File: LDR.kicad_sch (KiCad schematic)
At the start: 8 parts, among them J1101 LDR, J1102 ter, J1103 ter, U1101 LM393

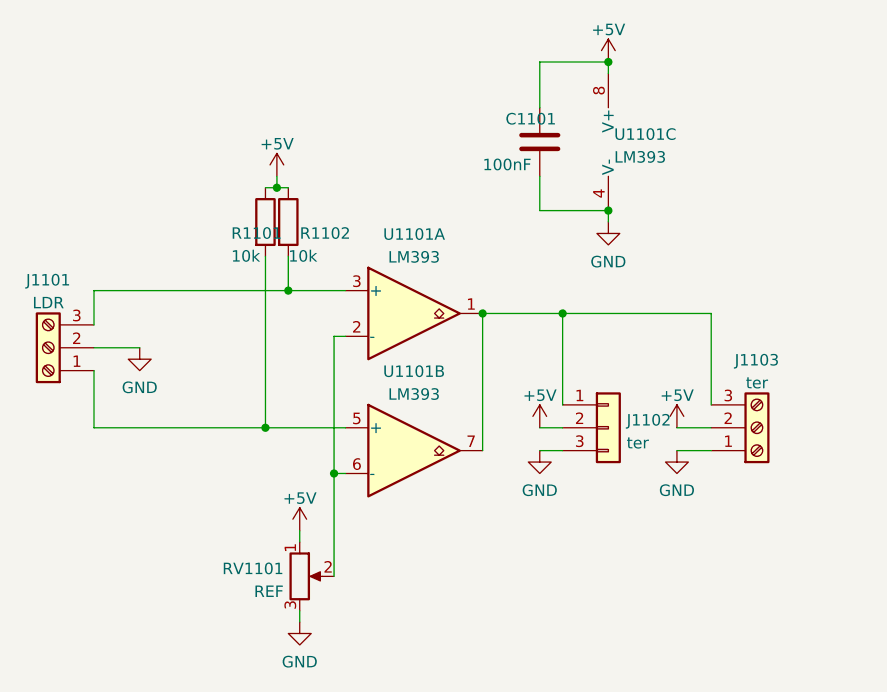
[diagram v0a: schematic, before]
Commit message: added hierarchial labels to some schematics
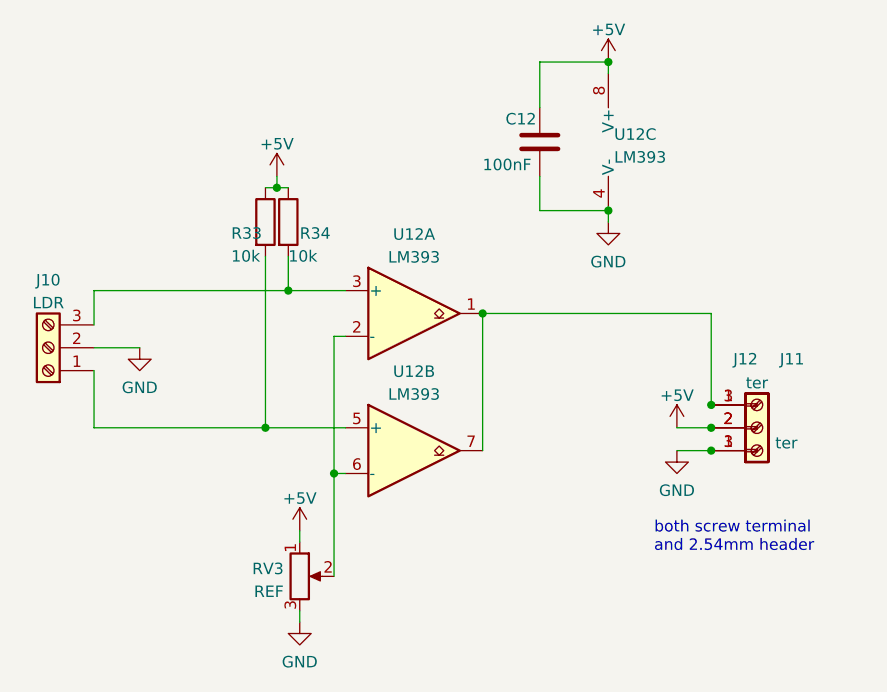
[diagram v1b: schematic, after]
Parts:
- renumbered C1101 to C12, J1101 to J10, J1102 to J11, J1103 to J12, R1101 to R33, R1102 to R34, RV1101 to RV3, U1101 to U12
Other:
- note added: "both screw terminal and 2.54mm header"
- moved on the sheet: J11

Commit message: moved some schematic scheets to their own folders and routed a board with it. This allow for re-use of PCB parts.
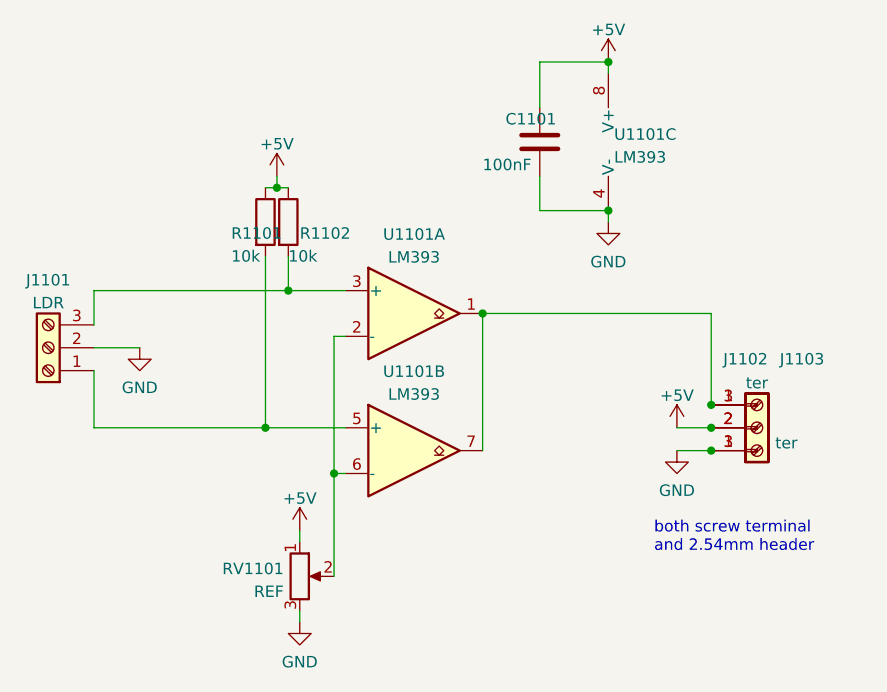
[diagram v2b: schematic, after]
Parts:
- renumbered C12 to C1101, J10 to J1101, J12 to J1102, J11 to J1103, R33 to R1101, R34 to R1102, RV3 to RV1101, U12 to U1101
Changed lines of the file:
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@@
   (symbol (lib_id "power:GND") (at 93.98 87.63 0) (unit 1)
     (in_bom yes) (on_board yes) (dnp no) (fields_autoplaced)
-    (property "Reference" "#PWR042" (at 93.98 93.98 0)
+    (property "Reference" "#PWR0132" (at 93.98 93.98 0)
       (effects (font (size 1.27 1.27)) hide)
     )
@@
       (project "general_schematics"
         (path "/e777d9ec-d073-4229-a9e6-2cf85636e407/38d599ac-34a4-48d6-818e-d419faf54082"
-          (reference "#PWR042") (unit 1)
+          (reference "#PWR0132") (unit 1)
         )
       )
@@
   (symbol (lib_id "power:+5V") (at 146.05 55.88 0) (unit 1)
     (in_bom yes) (on_board yes) (dnp no) (fields_autoplaced)
-    (property "Reference" "#PWR039" (at 146.05 59.69 0)
+    (property "Reference" "#PWR0126" (at 146.05 59.69 0)
       (effects (font (size 1.27 1.27)) hide)
     )
@@
       (project "general_schematics"
         (path "/e777d9ec-d073-4229-a9e6-2cf85636e407/38d599ac-34a4-48d6-818e-d419faf54082"
-          (reference "#PWR039") (unit 1)
+          (reference "#PWR0126") (unit 1)
         )
       )
@@
   (symbol (lib_id "power:GND") (at 153.67 99.06 0) (unit 1)
     (in_bom yes) (on_board yes) (dnp no) (fields_autoplaced)
-    (property "Reference" "#PWR046" (at 153.67 105.41 0)
+    (property "Reference" "#PWR0128" (at 153.67 105.41 0)
       (effects (font (size 1.27 1.27)) hide)
     )
@@
       (project "general_schematics"
         (path "/e777d9ec-d073-4229-a9e6-2cf85636e407/38d599ac-34a4-48d6-818e-d419faf54082"
-          (reference "#PWR046") (unit 1)
+          (reference "#PWR0128") (unit 1)
         )
       )
@@
   (symbol (lib_id "Device:C") (at 138.43 64.77 0) (unit 1)
     (in_bom yes) (on_board yes) (dnp no)
-    (property "Reference" "C12" (at 134.62 62.23 0)
+    (property "Reference" "C1101" (at 134.62 62.23 0)
       (effects (font (size 1.27 1.27)) (justify left))
     )
@@
       (project "general_schematics"
         (path "/e777d9ec-d073-4229-a9e6-2cf85636e407/38d599ac-34a4-48d6-818e-d419faf54082"
-          (reference "C12") (unit 1)
+          (reference "C1101") (unit 1)
         )
       )
@@
   (symbol (lib_id "Device:R") (at 107.95 73.66 0) (unit 1)
     (in_bom yes) (on_board yes) (dnp no)
-    (property "Reference" "R33" (at 104.14 74.93 0)
+    (property "Reference" "R1101" (at 104.14 74.93 0)
       (effects (font (size 1.27 1.27)) (justify left))
     )
@@
       (project "general_schematics"
         (path "/e777d9ec-d073-4229-a9e6-2cf85636e407/38d599ac-34a4-48d6-818e-d419faf54082"
-          (reference "R33") (unit 1)
+          (reference "R1101") (unit 1)
         )
       )
@@
   (symbol (lib_id "Connector:Screw_Terminal_01x03") (at 83.82 87.63 180) (unit 1)
     (in_bom yes) (on_board yes) (dnp no) (fields_autoplaced)
-    (property "Reference" "J10" (at 83.82 80.1202 0)
+    (property "Reference" "J1101" (at 83.82 80.1202 0)
       (effects (font (size 1.27 1.27)))
     )
@@
       (project "general_schematics"
         (path "/e777d9ec-d073-4229-a9e6-2cf85636e407/38d599ac-34a4-48d6-818e-d419faf54082"
-          (reference "J10") (unit 1)
+          (reference "J1101") (unit 1)
         )
       )
@@
   (symbol (lib_id "Connector:Screw_Terminal_01x03") (at 162.56 96.52 0) (mirror x) (unit 1)
     (in_bom yes) (on_board yes) (dnp no)
-    (property "Reference" "J12" (at 161.29 88.9 0)
+    (property "Reference" "J1102" (at 161.29 88.9 0)
       (effects (font (size 1.27 1.27)))
     )
@@
       (project "general_schematics"
         (path "/e777d9ec-d073-4229-a9e6-2cf85636e407/38d599ac-34a4-48d6-818e-d419faf54082"
-          (reference "J12") (unit 1)
+          (reference "J1102") (unit 1)
         )
       )
@@
   (symbol (lib_id "power:+5V") (at 111.76 107.95 0) (unit 1)
     (in_bom yes) (on_board yes) (dnp no) (fields_autoplaced)
-    (property "Reference" "#PWR047" (at 111.76 111.76 0)
+    (property "Reference" "#PWR0129" (at 111.76 111.76 0)
       (effects (font (size 1.27 1.27)) hide)
     )
@@
       (project "general_schematics"
         (path "/e777d9ec-d073-4229-a9e6-2cf85636e407/38d599ac-34a4-48d6-818e-d419faf54082"
-          (reference "#PWR047") (unit 1)
+          (reference "#PWR0129") (unit 1)
         )
       )
@@
   (symbol (lib_id "power:+5V") (at 153.67 96.52 0) (unit 1)
     (in_bom yes) (on_board yes) (dnp no) (fields_autoplaced)
-    (property "Reference" "#PWR044" (at 153.67 100.33 0)
+    (property "Reference" "#PWR0127" (at 153.67 100.33 0)
       (effects (font (size 1.27 1.27)) hide)
     )
@@
       (project "general_schematics"
         (path "/e777d9ec-d073-4229-a9e6-2cf85636e407/38d599ac-34a4-48d6-818e-d419faf54082"
-          (reference "#PWR044") (unit 1)
+          (reference "#PWR0127") (unit 1)
         )
       )
@@
   (symbol (lib_id "Connector_Generic:Conn_01x03") (at 162.56 96.52 0) (unit 1)
     (in_bom yes) (on_board yes) (dnp no)
-    (property "Reference" "J11" (at 165.1 88.9 0)
+    (property "Reference" "J1103" (at 165.1 88.9 0)
       (effects (font (size 1.27 1.27)) (justify left))
     )
@@
       (project "general_schematics"
         (path "/e777d9ec-d073-4229-a9e6-2cf85636e407/38d599ac-34a4-48d6-818e-d419faf54082"
-          (reference "J11") (unit 1)
+          (reference "J1103") (unit 1)
         )
       )
@@
   (symbol (lib_id "Comparator:LM393") (at 124.46 83.82 0) (unit 1)
     (in_bom yes) (on_board yes) (dnp no) (fields_autoplaced)
-    (property "Reference" "U12" (at 124.46 75.0402 0)
+    (property "Reference" "U1101" (at 124.46 75.0402 0)
       (effects (font (size 1.27 1.27)))
     )
@@
       (project "general_schematics"
         (path "/e777d9ec-d073-4229-a9e6-2cf85636e407/38d599ac-34a4-48d6-818e-d419faf54082"
-          (reference "U12") (unit 1)
+          (reference "U1101") (unit 1)
         )
       )
@@
   (symbol (lib_id "power:+5V") (at 109.22 68.58 0) (unit 1)
     (in_bom yes) (on_board yes) (dnp no) (fields_autoplaced)
-    (property "Reference" "#PWR040" (at 109.22 72.39 0)
+    (property "Reference" "#PWR0131" (at 109.22 72.39 0)
       (effects (font (size 1.27 1.27)) hide)
     )
@@
       (project "general_schematics"
         (path "/e777d9ec-d073-4229-a9e6-2cf85636e407/38d599ac-34a4-48d6-818e-d419faf54082"
-          (reference "#PWR040") (unit 1)
+          (reference "#PWR0131") (unit 1)
         )
       )
@@
   (symbol (lib_id "Comparator:LM393") (at 148.59 64.77 0) (unit 3)
     (in_bom yes) (on_board yes) (dnp no) (fields_autoplaced)
-    (property "Reference" "U12" (at 146.685 63.9353 0)
+    (property "Reference" "U1101" (at 146.685 63.9353 0)
       (effects (font (size 1.27 1.27)) (justify left))
     )
@@
       (project "general_schematics"
         (path "/e777d9ec-d073-4229-a9e6-2cf85636e407/38d599ac-34a4-48d6-818e-d419faf54082"
-          (reference "U12") (unit 3)
+          (reference "U1101") (unit 3)
         )
       )
@@
   (symbol (lib_id "Comparator:LM393") (at 124.46 99.06 0) (unit 2)
     (in_bom yes) (on_board yes) (dnp no) (fields_autoplaced)
-    (property "Reference" "U12" (at 124.46 90.2802 0)
+    (property "Reference" "U1101" (at 124.46 90.2802 0)
       (effects (font (size 1.27 1.27)))
     )
@@
       (project "general_schematics"
         (path "/e777d9ec-d073-4229-a9e6-2cf85636e407/38d599ac-34a4-48d6-818e-d419faf54082"
-          (reference "U12") (unit 2)
+          (reference "U1101") (unit 2)
         )
       )
@@
   (symbol (lib_id "Device:R_Potentiometer") (at 111.76 113.03 0) (unit 1)
     (in_bom yes) (on_board yes) (dnp no) (fields_autoplaced)
-    (property "Reference" "RV3" (at 109.982 112.1953 0)
+    (property "Reference" "RV1101" (at 109.982 112.1953 0)
       (effects (font (size 1.27 1.27)) (justify right))
     )
@@
       (project "general_schematics"
         (path "/e777d9ec-d073-4229-a9e6-2cf85636e407/38d599ac-34a4-48d6-818e-d419faf54082"
-          (reference "RV3") (unit 1)
+          (reference "RV1101") (unit 1)
         )
       )
@@
   (symbol (lib_id "Device:R") (at 110.49 73.66 0) (unit 1)
     (in_bom yes) (on_board yes) (dnp no)
-    (property "Reference" "R34" (at 111.76 74.93 0)
+    (property "Reference" "R1102" (at 111.76 74.93 0)
       (effects (font (size 1.27 1.27)) (justify left))
     )
@@
       (project "general_schematics"
         (path "/e777d9ec-d073-4229-a9e6-2cf85636e407/38d599ac-34a4-48d6-818e-d419faf54082"
-          (reference "R34") (unit 1)
+          (reference "R1102") (unit 1)
         )
       )
@@
   (symbol (lib_id "power:GND") (at 146.05 73.66 0) (unit 1)
     (in_bom yes) (on_board yes) (dnp no) (fields_autoplaced)
-    (property "Reference" "#PWR041" (at 146.05 80.01 0)
+    (property "Reference" "#PWR0125" (at 146.05 80.01 0)
       (effects (font (size 1.27 1.27)) hide)
     )
@@
       (project "general_schematics"
         (path "/e777d9ec-d073-4229-a9e6-2cf85636e407/38d599ac-34a4-48d6-818e-d419faf54082"
-          (reference "#PWR041") (unit 1)
+          (reference "#PWR0125") (unit 1)
         )
       )
@@
   (symbol (lib_id "power:GND") (at 111.76 118.11 0) (unit 1)
     (in_bom yes) (on_board yes) (dnp no) (fields_autoplaced)
-    (property "Reference" "#PWR048" (at 111.76 124.46 0)
+    (property "Reference" "#PWR0130" (at 111.76 124.46 0)
       (effects (font (size 1.27 1.27)) hide)
     )
@@
       (project "general_schematics"
         (path "/e777d9ec-d073-4229-a9e6-2cf85636e407/38d599ac-34a4-48d6-818e-d419faf54082"
-          (reference "#PWR048") (unit 1)
-        )
-      )
+          (reference "#PWR0130") (unit 1)
+        )
+      )
